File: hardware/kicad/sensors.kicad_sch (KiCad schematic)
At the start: 28 parts, among them J3 JST SM06B-GHS-TB (SEN66-SIN-T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, J4 1x5 P1.27mm through-hole head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, U4 MIKROE-2462 NFC Tag 2 Click (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

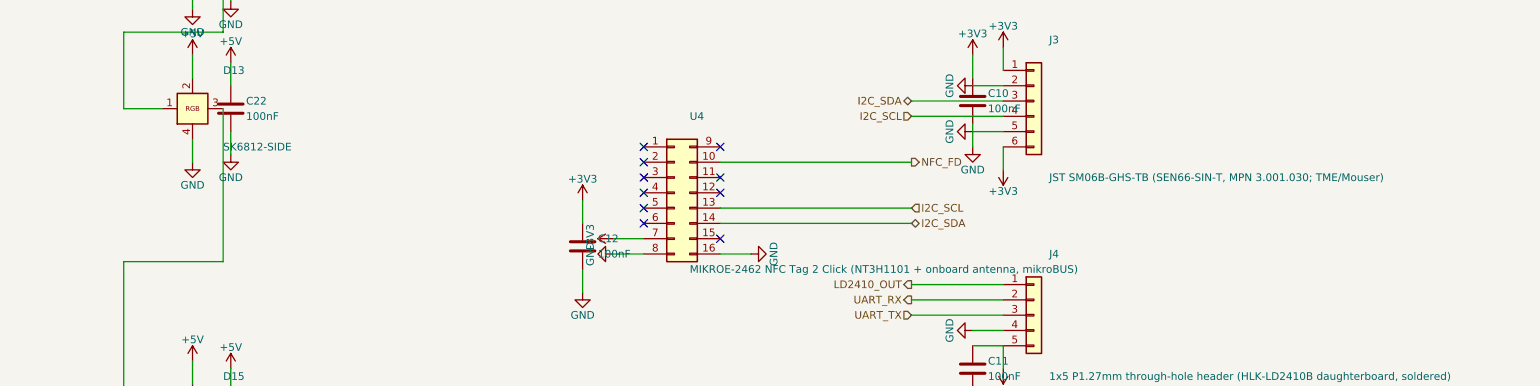
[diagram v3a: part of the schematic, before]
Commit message: kicad+docs: v0.21 - M3 closure (J5/J6/J7/J8 schematic) + UART/USB crossover fix
M3 part 1 (MCU): replace U3 placeholder with J5 + J6 schematic symbols
(Conn_01x15 each). J5 = ESP32 J1 antenna-side row (pin tips left,
angle=0); J6 = ESP32 J3 USB-side row (pin tips right, angle=180). Pin
numbers 1..15 match PCB pad numbering 1:1. All 7 OAS signal pins get
hier-label stubs; 5 GND pins get power flags; 13 NC pins get
no_connect markers. J2 DNP recovery header rotated 180 so its TX/RX
pin row aligns with J6 UART_TX/RX.

M3 part 2 (Sensors): replace U4 mikroBUS placeholder with J7 + J8
schematic symbols (Conn_01x08 each). J7 = mikroBUS pins 1..8 (LEFT
column, angle=0); J8 = mikroBUS pins 9..16 (RIGHT column, angle=180).
J7 pin 7 = +3V3, J7 pin 8 = GND, J8 pin 2 = NFC_FD, J8 pin 5 = SCL,
J8 pin 6 = SDA, J8 pin 8 = GND; 10 unused pins get no_connect markers.

Root-sheet UART/USB crossover bug fixed (pre-existing v0.20 finding):
the UART_TX east-from-sensors wire ran at Y=97.79 in the same column
as the IO sub-sheet's USB_DP west-into-io wire (also at Y=97.79),
overlapping in X range [101.6, 143.51] and bridging UART_TX into
USB_DP. Same pattern for UART_RX/EN at Y=100.33. Fix re-routes UART
east stubs south of the IO block before going east (Y=110.49 for
UART_TX, Y=113.03 for UART_RX), eliminating the Y collision. Verified
clean: /MCU/UART_TX = {J2.3, J4.3, J6.2}, /MCU/UART_RX = {J2.4, J4.2,
J6.3}, /IO/USB_DP / EN no longer contain LD2410 or UART pins.

SEN66 mech-ref F.CrtYd removed (5 of 15 v0.20 DRC violations were
false-positive courtyards_overlap between SENS1 body and PCB-surface
SMD parts; SEN66 floats 21.5 mm above PCB so the 2D courtyard rule
doesn't reflect physical clearance). Matches the existing convention
in _emit_daughterboard_reference_pcb_footprint() (MOD1/MOD2).

Net coverage: 216 pad-net assignments applied by
sync_pcb_nets_from_schematic (up from 188 in v0.20). All J5..J8
sockets fully assigned. DRC: 10 violations (down from 15) - 1
courtyards_overlap C4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
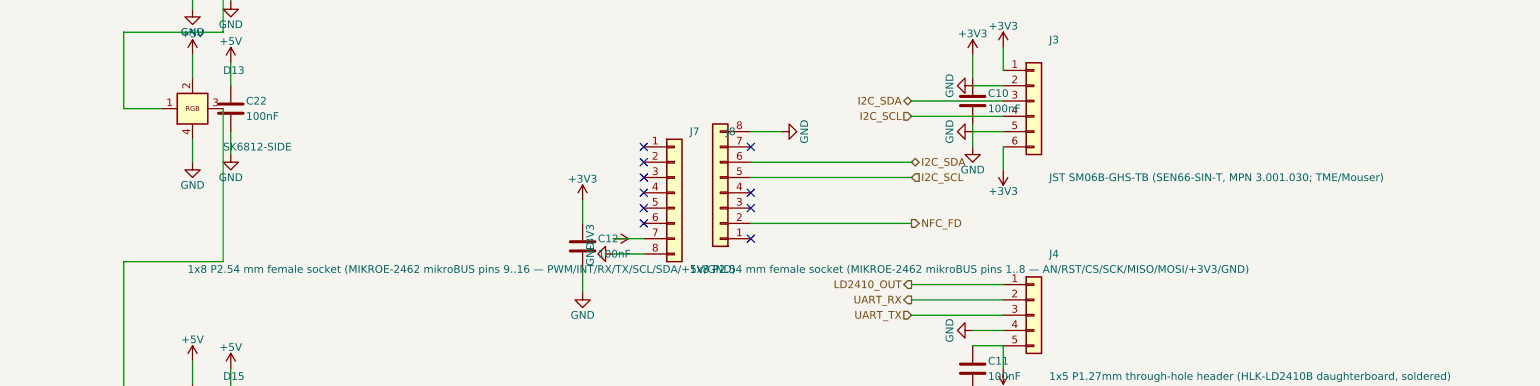
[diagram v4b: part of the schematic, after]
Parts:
- removed U4: MIKROE-2462 NFC Tag 2 Click (NT3H1101 + onboard a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, symbol Connector_Generic:Conn_02x08_Top_Bottom
- added J7, J8: 1x8 P2.54 mm female socket (MIKROE-2462 mikroBUS 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, symbol Connector_Generic:Conn_01x08
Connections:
- net +3V3: now also J7.7 (Pin_7)
- net GND: now also J7.8 (Pin_8), J8.8 (Pin_8)
- net I2C_SCL: now also J8.5 (Pin_5)
- net I2C_SDA: now also J8.6 (Pin_6)
- net NFC_FD: now also J8.2 (Pin_2)
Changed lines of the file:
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@@
 (symbol
 	(lib_id "power:+3V3")
-	(at 110.49 133.35 90)
+	(at 110.49 133.35 270)
 	(unit 1)
 	(exclude_from_sim no)
@@
 (wire
 	(pts
-		(xy 128.27 120.65) (xy 160.02 120.65)
+		(xy 133.35 130.81) (xy 160.02 130.81)
 	)
 	(stroke
@@
 (hierarchical_label "NFC_FD"
 	(shape output)
+	(at 160.02 130.81 0)
+	(effects
+		(font
+			(size 1.27 1.27)
+		)
+		(justify left)
+	)
+)
+(wire
+	(pts
+		(xy 133.35 123.19) (xy 160.02 123.19)
+	)
+	(stroke
+		(width 0)
+		(type default)
+	)
+)
+(hierarchical_label "I2C_SCL"
+	(shape input)
+	(at 160.02 123.19 0)
+	(effects
+		(font
+			(size 1.27 1.27)
+		)
+		(justify left)
+	)
+)
+(wire
+	(pts
+		(xy 133.35 120.65) (xy 160.02 120.65)
+	)
+	(stroke
+		(width 0)
+		(type default)
+	)
+)
+(hierarchical_label "I2C_SDA"
+	(shape bidirectional)
 	(at 160.02 120.65 0)
 	(effects
@@
 (wire
 	(pts
-		(xy 128.27 128.27) (xy 160.02 128.27)
-	)
-	(stroke
-		(width 0)
-		(type default)
-	)
-)
-(hierarchical_label "I2C_SCL"
-	(shape input)
-	(at 160.02 128.27 0)
-	(effects
-		(font
-			(size 1.27 1.27)
-		)
-		(justify left)
-	)
-)
-(wire
-	(pts
-		(xy 128.27 130.81) (xy 160.02 130.81)
-	)
-	(stroke
-		(width 0)
-		(type default)
-	)
-)
-(hierarchical_label "I2C_SDA"
-	(shape bidirectional)
-	(at 160.02 130.81 0)
-	(effects
-		(font
-			(size 1.27 1.27)
-		)
-		(justify left)
-	)
-)
-(wire
-	(pts
-		(xy 128.27 135.89) (xy 133.35 135.89)
+		(xy 133.35 115.57) (xy 138.43 115.57)
 	)
 	(stroke
@@
 (symbol
 	(lib_id "power:GND")
-	(at 133.35 135.89 90)
+	(at 138.43 115.57 90)
 	(unit 1)
 	(exclude_from_sim no)
@@
 	(fields_autoplaced yes)
 	(property "Reference" "#PWR52"
-		(at 133.35 132.08 0)
+		(at 138.43 111.76 0)
 		(effects
 			(font
@@
 	)
 	(property "Value" "GND"
-		(at 137.16 135.89 0)
+		(at 142.24 115.57 0)
 		(effects
 			(font
@@
 	)
 	(property "Footprint" ""
-		(at 133.35 135.89 0)
+		(at 138.43 115.57 0)
 		(effects
 			(font
@@
 	)
 	(property "Datasheet" ""
-		(at 133.35 135.89 0)
+		(at 138.43 115.57 0)
 		(effects
 			(font
@@
 	)
 	(property "Description" ""
-		(at 133.35 135.89 0)
+		(at 138.43 115.57 0)
 		(effects
 			(font
@@
 )
 (no_connect
-	(at 128.27 118.11)
-)
-(no_connect
-	(at 128.27 123.19)
-)
-(no_connect
-	(at 128.27 125.73)
-)
-(no_connect
-	(at 128.27 133.35)
+	(at 133.35 133.35)
+)
+(no_connect
+	(at 133.35 128.27)
+)
+(no_connect
+	(at 133.35 125.73)
+)
+(no_connect
+	(at 133.35 118.11)
 )
 (wire
@@
 )
         	(symbol
-        		(lib_id "Connector_Generic:Conn_02x08_Top_Bottom")
+        		(lib_id "Connector_Generic:Conn_01x08")
         		(at 120.65 125.73 0)
         		(unit 1)
@@
         		(dnp no)
         		(fields_autoplaced yes)
-        		(property "Reference" "U4"
-        			(at 123.19 113.03 0)
+        		(property "Reference" "J7"
+        			(at 123.19 115.57 0)
         			(effects
         				(font
@@
         			)
         		)
-        		(property "Value" "MIKROE-2462 NFC Tag 2 Click (NT3H1101 + onboard antenna, mikroBUS)"
+        		(property "Value" "1x8 P2.54 mm female socket (MIKROE-2462 mikroBUS pins 1..8 — AN/RST/CS/SCK/MISO/MOSI/+3V3/GND)"
         			(at 123.19 138.43 0)
         			(effects
@@
         			)
         		)
-        		(property "Datasheet" "https://www.mikroe.com/nfc-tag-2-click"
+        		(property "Datasheet" ""
         			(at 120.65 125.73 0)
         			(effects
@@
         			)
         		)
-        		(property "Description" "mikroBUS 2x8 socket — MIKROE-2462 NFC Tag 2 Click daughterboard (NT3H1101 NTAG I²C plus + onboard PCB antenna)"
+        		(property "Description" ""
         			(at 120.65 125.73 0)
         			(effects
@@
 		)
 		(pin "8"
-		)
-		(pin "9"
-		)
-		(pin "10"
-		)
-		(pin "11"
-		)
-		(pin "12"
-		)
-		(pin "13"
-		)
-		(pin "14"
-		)
-		(pin "15"
-		)
-		(pin "16"
 		)
         		(instances
         			(project "oas"
         				(path "/515343fe-5590-5fd9-97ec-5bed0f979de2/a5e13d4c-9fec-5607-b893-c0f069874d1d"
-        					(reference "U4")
+        					(reference "J7")
         					(unit 1)
         				)
+        			)
+        		)
+        	)
+        	(symbol
+        		(lib_id "Connector_Generic:Conn_01x08")
+        		(at 128.27 125.73 180)
+        		(unit 1)
+        		(exclude_from_sim no)
+        		(in_bom yes)
+        		(on_board yes)
+        		(dnp no)
+        		(fields_autoplaced yes)
+        		(property "Reference" "J8"
+        			(at 130.81 115.57 0)
+        			(effects
+        				(font
+        					(size 1.27 1.27)
+        				)
+        				(justify left)
+        			)
+        		)
+        		(property "Value" "1x8 P2.54 mm female socket (MIKROE-2462 mikroBUS pins 9..16 — PWM/INT/RX/TX/SCL/SDA/+5V/GND)"
+        			(at 130.81 138.43 0)
+        			(effects
+        				(font
+        					(size 1.27 1.27)
+        				)
+        				(justify left)
+        			)
+        		)
+        		(property "Footprint" ""
+        			(at 128.27 125.73 0)
+        			(effects
+        				(font
+        					(size 1.27 1.27)
+        				)
+        				(hide yes)
+        			)
+        		)
+        		(property "Datasheet" ""
+        			(at 128.27 125.73 0)
+        			(effects
+        				(font
+        					(size 1.27 1.27)
+        				)
+        				(hide yes)
+        			)
+        		)
+        		(property "Description" ""
+        			(at 128.27 125.73 0)
+        			(effects
+        				(font
+        					(size 1.27 1.27)
+        				)
+        				(hide yes)
+        			)
+        		)
+        		(pin "1"
+		)
+		(pin "2"
+		)
+		(pin "3"
+		)
+		(pin "4"
+		)
+		(pin "5"
+		)
+		(pin "6"
+		)
+		(pin "7"
+		)
+		(pin "8"
+		)
+        		(instances
+        			(project "oas"
+        				(path "/515343fe-5590-5fd9-97ec-5bed0f979de2/a5e13d4c-9fec-5607-b893-c0f069874d1d"
+        					(reference "J8")
+        					(unit 1)
+        				)

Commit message: kicad+docs: v0.24 - fix v0.23 regressions (lib-qualify footprints + ERC strict)
Closes review iteration 2 findings (`_review-iteration-2-v0.23.md`):

1. Mn3 V3 regression — lib-qualify footprint back-fill.
   `_build_pcb_ref_to_footprint()` now lib-qualifies bare PCB-side
   Footprint property values via a new `BARE_FOOTPRINT_TO_LIB` table
   (12 entries) and asserts every returned value contains `:`. In
   parallel, the inline `gen_*_pcb_footprint` generators that emitted
   bare names now write fully-qualified `Lib:Name` strings directly
   (`Capacitor_SMD:C_0402_1005Metric`, `Package_TO_SOT_SMD:SOT-23`,
   `Inductor_SMD:L_APV_ANR5040`, `Fuse:Fuse_2920_7451Metric`,
   `Capacitor_THT:CP_Radial_D8.0mm_P3.50mm`, etc.). 15 ERC
   `footprint_link_issues` warnings → 0.

2. Mj2 — `regenerate.py` ERC strict mode. `kicad-cli sch erc` now
   invoked with `--severity-error --severity-warning
   --exit-code-violations`, mirroring DRC strictness. Verified by
   corrupting a schematic Footprint property and confirming abort.
   CLAUDE.md "PCB design workflow" §3 ("aborts on any error or
   warning") is now actually enforced for ERC, not just DRC.

3. C1 V4 — derived `.kicad_pcb` / `.kicad_sch` resynced with
   `generate.py`. The v0.23 commit shipped `generate.py` updates
   without regenerating the derived files; this commit brings them
   into sync via `python regenerate.py`.

4. Mj1 — CLAUDE.md v0.23 changelog entry added retroactively
   (had been missing). v0.24 entry added documenting this fix
   series + the ERC-strictness lesson.

5. `hardware/components/_review-iteration-2-v0.23.md` committed
   (previously untracked).

DRC = 0 violations / 0 warnings.
ERC = 0 violations / 0 warnings (now strict).
Determinism self-check passes (17 files bit-identical across two
consecutive `regenerate.py` runs).

Co-Authored-By: Claude Opus 4.7 (1M context) <noreply@anthropic.com>
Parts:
- C20, C21, C22, C24, C25, C26, C27, C28, C29, C30, C31: footprint (none) -> Capacitor_SMD:C_0402_1005Metric
- J3: footprint (none) -> Connector_JST:JST_GH_SM06B-GHS-TB_1x06-1MP_P1.25mm_Horizontal
- J4: footprint (none) -> Connector_PinHeader_1.27mm:PinHeader_1x05_P1.27mm_Vertical
- J7, J8: footprint (none) -> Connector_PinSocket_2.54mm:PinSocket_1x08_P2.54mm_Vertical
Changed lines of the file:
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@@
         			)
         		)
-        		(property "Footprint" ""
+        		(property "Footprint" "Connector_JST:JST_GH_SM06B-GHS-TB_1x06-1MP_P1.25mm_Horizontal"
         			(at 180.34 110.49 0)
         			(effects
@@
         			)
         		)
-        		(property "Footprint" ""
+        		(property "Footprint" "Connector_PinHeader_1.27mm:PinHeader_1x05_P1.27mm_Vertical"
         			(at 180.34 146.05 0)
         			(effects
@@
         			)
         		)
-        		(property "Footprint" ""
+        		(property "Footprint" "Connector_PinSocket_2.54mm:PinSocket_1x08_P2.54mm_Vertical"
         			(at 120.65 125.73 0)
         			(effects
@@
         			)
         		)
-        		(property "Footprint" ""
+        		(property "Footprint" "Connector_PinSocket_2.54mm:PinSocket_1x08_P2.54mm_Vertical"
         			(at 128.27 125.73 0)
         			(effects
@@
 		)
 	)
-	(property "Footprint" ""
+	(property "Footprint" "Capacitor_SMD:C_0402_1005Metric"
 		(at 46.99 60.96 0)
 		(effects
@@
 		)
 	)
-	(property "Footprint" ""
+	(property "Footprint" "Capacitor_SMD:C_0402_1005Metric"
 		(at 46.99 86.36 0)
 		(effects
@@
 		)
 	)
-	(property "Footprint" ""
+	(property "Footprint" "Capacitor_SMD:C_0402_1005Metric"
 		(at 46.99 111.76 0)
 		(effects
@@
 		)
 	)
-	(property "Footprint" ""
+	(property "Footprint" "Capacitor_SMD:C_0402_1005Metric"
 		(at 46.99 162.56 0)
 		(effects
@@
 		)
 	)
-	(property "Footprint" ""
+	(property "Footprint" "Capacitor_SMD:C_0402_1005Metric"
 		(at 46.99 187.96 0)
 		(effects
@@
 		)
 	)
-	(property "Footprint" ""
+	(property "Footprint" "Capacitor_SMD:C_0402_1005Metric"
 		(at 46.99 213.36 0)
 		(effects
@@
 		)
 	)
-	(property "Footprint" ""
+	(property "Footprint" "Capacitor_SMD:C_0402_1005Metric"
 		(at 46.99 238.76 0)
 		(effects
@@
 		)
 	)
-	(property "Footprint" ""
+	(property "Footprint" "Capacitor_SMD:C_0402_1005Metric"
 		(at 46.99 264.16 0)
 		(effects
@@
 		)
 	)
-	(property "Footprint" ""
+	(property "Footprint" "Capacitor_SMD:C_0402_1005Metric"
 		(at 46.99 289.56 0)
 		(effects
@@
 		)
 	)
-	(property "Footprint" ""
+	(property "Footprint" "Capacitor_SMD:C_0402_1005Metric"
 		(at 46.99 314.96 0)
 		(effects
@@
 		)
 	)
-	(property "Footprint" ""
+	(property "Footprint" "Capacitor_SMD:C_0402_1005Metric"
 		(at 46.99 340.36 0)
 		(effects

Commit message: kicad: v0.25 - widen Mn3 back-fill regex to capture indented footprint blocks
Closes review-iteration-3 (Mn3-residual + Nt-doc-comment) at v0.24:

- _build_pcb_ref_to_footprint() regex (?m)^\(footprint "..." widened to
  (?m)^\s*\(footprint "..." . KiCad pretty-prints some (footprint ...) blocks
  in oas.kicad_pcb with leading tab/space indentation; the column-0 anchor
  silently skipped 31 of 76 placed footprints in v0.24, leaving 27 schematic
  real-component symbols with empty Footprint properties (ERC-silent but
  cosmetically wrong). Match count: 45 -> 76 (exactly equal to kiutils
  enumeration). Verified no nested (footprint "..." references exist.
- Inner re.match relaxed to re.search since sliced blocks can begin with
  whitespace.
- Docstring updated to disclose the regex behavior honestly (closes
  Nt-doc-comment from review iter-3).
- All 65 real-component schematic instances now carry a fully-qualified
  Lib:Name Footprint property. Empty-Footprint count: 0 (was 27 at v0.24,
  51 at v0.22). Previously-missed refs now lib-qualified: C2 + C5-C17, D1-D3,
  F1, L1-L2, R1-R7, plus ZT1-ZT4.
- DRC = 0/0, ERC = 0/0, determinism self-check passes (17 files bit-identical
  across two consecutive runs). PCB geometry unchanged - schematic-side
  .kicad_sch diffs only.
- Adds the iteration-3 review file (hardware/components/_review-iteration-3-v0.24.md).

Co-Authored-By: Claude Opus 4.7 (1M context) <noreply@anthropic.com>
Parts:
- C10, C11, C12: footprint (none) -> Capacitor_SMD:C_0603_1608Metric
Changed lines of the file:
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@@
 		)
 	)
-	(property "Footprint" ""
+	(property "Footprint" "Capacitor_SMD:C_0603_1608Metric"
 		(at 170.18 110.49 0)
 		(effects
@@
 		)
 	)
-	(property "Footprint" ""
+	(property "Footprint" "Capacitor_SMD:C_0603_1608Metric"
 		(at 170.18 154.94 0)
 		(effects
@@
 		)
 	)
-	(property "Footprint" ""
+	(property "Footprint" "Capacitor_SMD:C_0603_1608Metric"
 		(at 105.41 134.62 0)
 		(effects

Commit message: kicad+bom: v0.38 - swarm audit v2 fixes (BOM-project coupling + silk polish)
30-agent read-only re-audit confirmed all v0.35-v0.37 CRITICAL fixes
in place and identified 6 follow-up items + 1 false positive. Applied
fixes:

Schematic ↔ BOM coupling (audit-16, primary user concern):
- generate.py: new _build_lcsc_metadata_map() + _apply_schematic_lcsc_metadata()
  injects Manufacturer / MPN / LCSC properties on every component symbol
  whose (Value, Footprint) matches a row in hardware/bom/lcsc-mapping.csv.
  Closes "projekt sobie, BOM sobie" — schematic is now self-sufficient
  for BOM export.
- export_production.py: BOM export switched to native kicad-cli --fields
  emitting Manufacturer + MPN columns directly from schematic. Post-process
  preserves them and adds JLCPCB_Library classification.
- New BOM CSV columns: Comment, Designator, Footprint, Manufacturer, MPN,
  LCSC, JLCPCB_Library, Qty.

Silkscreen polish (audit-26 / -27 / -24 / -28 / agent-08+11+30):
- D3 descriptor drift: 18V Zener → 10V Zener across generate.py PCB descr
  + 5 inline design comments (schematic Value + lcsc-mapping were already
  correct at v0.37; this fix syncs the source-of-truth comments).
- Radial cap "+" polarity marks: moved from pad_x+1.4 (INSIDE body radius,
  hidden post-assembly) to body_r+0.7 (~0.7 mm outside body, visible after
  the 8/6.3 mm cap solders down).
- SK6812 LED pin-1 dot: moved from F.Fab → F.SilkS in both lib generator
  and PCB-side footprint emitter, so the ring orientation is verifiable
  on physical PCB without consulting the assembly drawing.
- U1 LM2596S TO-263-5: added F.SilkS pin-1 dot at (-4.5, +1.5) radius 0.4
  for hand-assembly orientation.
- Board ID labels on F.SilkS: "Open Ambient Sensor" + "OAS v0.38" in the
  clear strip between MIKROE east edge (-12.7) and C3 cutout west (+4.9).
  Full repo URL on F.Fab (visible in renders, not silk-printed — URL too
  long for the strip at the 1.0 mm silk_min_text_height rule).

False positive confirmed (audit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
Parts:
- C10, C11, C12: LCSC (none) -> C14663; MPN (none) -> CC0603KRX7R9BB104; Manufacturer (none) -> Yageo
- C20, C21, C22, C24, C25, C26, C27, C28, C29, C30, C31: LCSC (none) -> C1525; MPN (none) -> CL05B104KO5NNNC; Manufacturer (none) -> Samsung Electro-Mechanics
- D11, D12, D13, D15, D16, D17, D18, D19, D20, D21, D22: LCSC (none) -> C5378721; MPN (none) -> SK6812SIDE-A; Manufacturer (none) -> OPSCO Optoelectronics
- J3: LCSC (none) -> C133065; MPN (none) -> SM06B-GHS-TB(LF)(SN); Manufacturer (none) -> JST Sales America
